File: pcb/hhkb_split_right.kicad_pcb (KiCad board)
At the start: 2 copper layers, 173.7 x 97.4 mm, 83 parts, among them SW1 6, SW10 Y, SW11 U, SW12 I, SW13 O, SW14 P, SW15 [, SW16 ], SW17 Del, SW18 H, SW19 J, SW2 7, SW20 K, SW21 L, SW22 ;, SW23 ', SW24 Enter, SW25 N, SW26 M, SW27 ,, SW28 ., SW29 /, SW3 8, SW30 Shift, SW31 Fn, SW32 R-Space, SW33 Meta, SW34 Alt, SW4 9, SW5 0, SW6 -, SW7 =, SW8 \, SW9 `, U1 74LVC595, U2 74LVC595

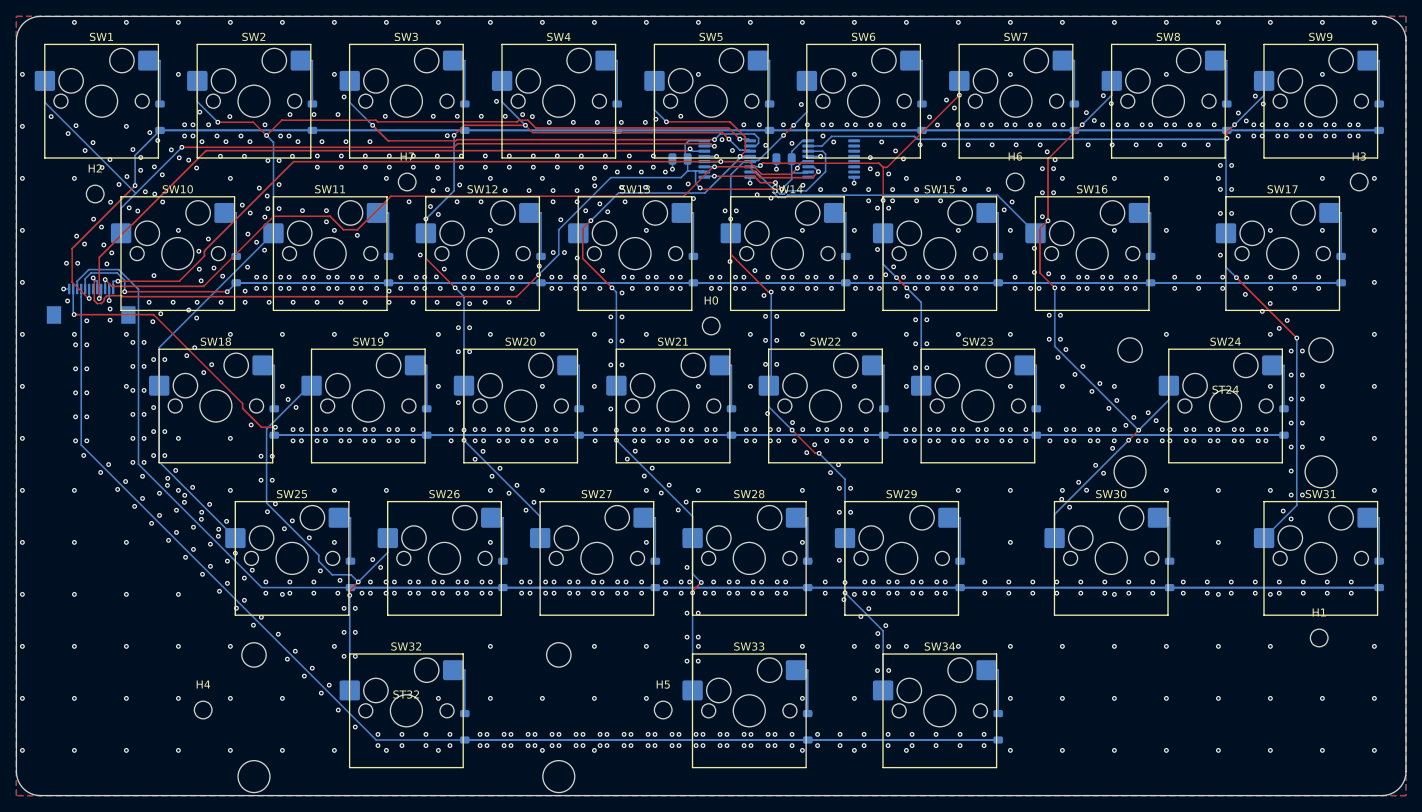
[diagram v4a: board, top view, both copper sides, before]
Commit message: 子基板の配線を外周へ逃がし、電源部の向きを流れに合わせた
利用者が絵で示した「電源は盤面の外周を使い、中央を空ける」という
方針を実装した回。**私は数字だけ追っていて、絵を見た利用者の指摘の
ほうが毎回早く核心に届いた。**

■ 外周レーン（利用者「両側 2 ピンぐらいは外側から回せるのでは」）

  XIAO のパッド列（±7.62）の外に **2.03mm** ある。ここへ 2 本/側を
  逃がし、内側レーンを 5 本 → 2 本に減らした。

  ⚠️ **刻みはビアの径で決まる。**最初 0.4mm（配線の幅）で 3 本置いて
  DRC 13 件。φ0.6 + クリアランス 0.2 = **0.80mm 必要**で 2 本/側が上限。

  ⚠️ **ビアを省いて裏面のまま走らせる案は駄目。**間隔 0.40mm で 3 本
  入る（外周に裏面部品は無い）が、**層の分離を失う**。内側レーンへ
  向かう横枝は B.Cu なので、外側も B.Cu だと必ず交差する（実測 12 件）。
  **ビアは無駄ではなく、層を分けるために要る。**

■ 真下パス（利用者「D6/D7 は横向きでなく下向きに伸ばせる」）

  FFC に最も近い 1 本は、パッド列の x のまま真下へ降ろす。
  レーンもビアも使わない。ROW2 18.9→16.8mm、CS 18.4→16.2mm。

  ⚠️ 条件を `|x| > 7.0` で書いて**全パッドが該当**し、20mm の配線が
  盤面を横断して DRC 38 件。正しくは「その列で FFC に最も近い 1 本」
  ＝ i == 0。

■ 部品の向き（利用者「バルクの向きが逆」「電源周りこんな感じで」）

  - C_BULK: 縦置き（x 方向 1.4mm 節約）＋ **+90°**。XIAO は 3V3 が
    手前(9.59)・GND が奥(12.13) なので、同じ並びにして平行に届かせる
  - R_LO: 180°。SENSE が R_HI 側（左）を向き、分圧の中点が隣り合う
  - SW_PWR: 中央の縦帯（x ±0.9）を空ける。GND スティッチングが使う

■ 配線長

  子基板の合計 218.5 → **205.1mm**

DRC: 左 違反3/未配線0 / 右 違反2/未配線0 / 子基板 違反6/未配線1
（主基板は**両方とも未配線 0**。子基板の 6 件は下記）
test_circuit・test_daughterboard・test_keyscan・test_schematic・
test_pinmap = 81 件通過。**pytest tools 全体は未実行。**

Co-Authored-By: Claude Opus 5 (1M context) <noreply@anthropic.com>
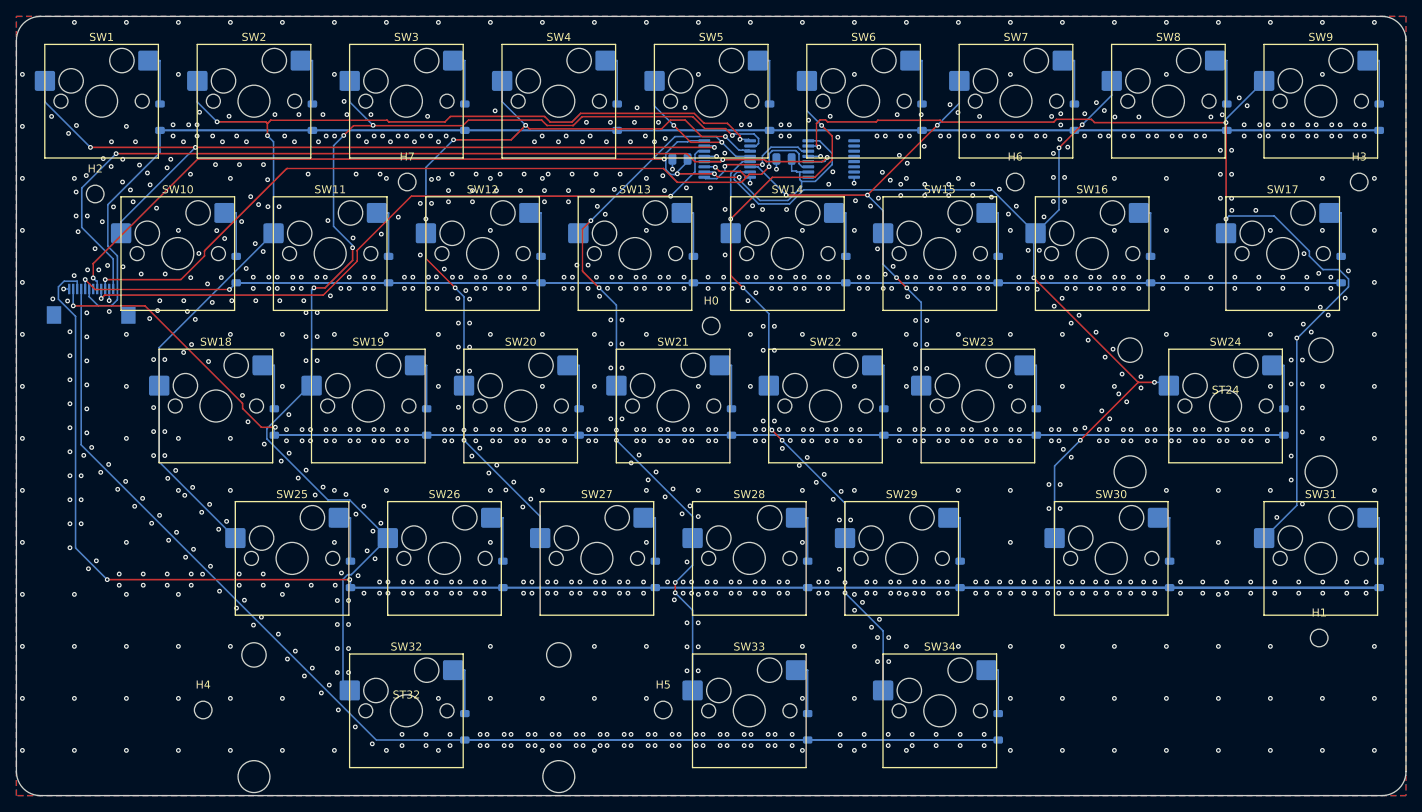
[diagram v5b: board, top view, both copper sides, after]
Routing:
- net ROW3: track 322.2 -> 383.6 mm, vias 0 -> 2
- net COL2: track 112.3 -> 150.4 mm, vias 4 -> 5
- net ROW4: track 239.9 -> 258.9 mm
- net CS: track 97.9 -> 115.2 mm
- net COL8: track 117.3 -> 133.3 mm
- net COL5: track 91.5 -> 104.3 mm, vias 8 -> 7
- net V3V3: track 118.6 -> 126.6 mm, vias 4 -> 5
- net U1_U2: track 22.3 -> 15.9 mm
- net SPI_SCK: track 102.0 -> 105.9 mm
- net COL0: track 100.8 -> 104.6 mm, vias 2 -> 3
- net COL4: track 110.4 -> 107.6 mm
- net ROW0: track 332.5 -> 334.4 mm, vias 2 -> 0
- net ROW1: track 298.9 -> 297.1 mm
- net COL1: track 136.0 -> 137.8 mm
- net SPI_MOSI: track 87.8 -> 86.3 mm
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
